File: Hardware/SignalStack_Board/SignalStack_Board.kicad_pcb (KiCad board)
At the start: 2 copper layers, 101.6 x 67.6 mm, 66 parts, among them J1 Molex_uF_SV_06, J2 RJ45_LED_Shielded, J3 Molex_uF_SV_06, Q1 SI4156DY, Q2 SI4156DY, Q3 SI4156DY, Q4 SI4156DY, Q5 SI4156DY, Q6 SI4156DY, Q7 SI4156DY, Q8 SI4156DY, U1 OKI, U2 SMAJ12CA, U3 Teensy4.1_DEV-16771, U4 TSR_1-2450, U5 IRS2005S, U6 IRS2005S, U8 IRS2005S, U9 IRS2005S

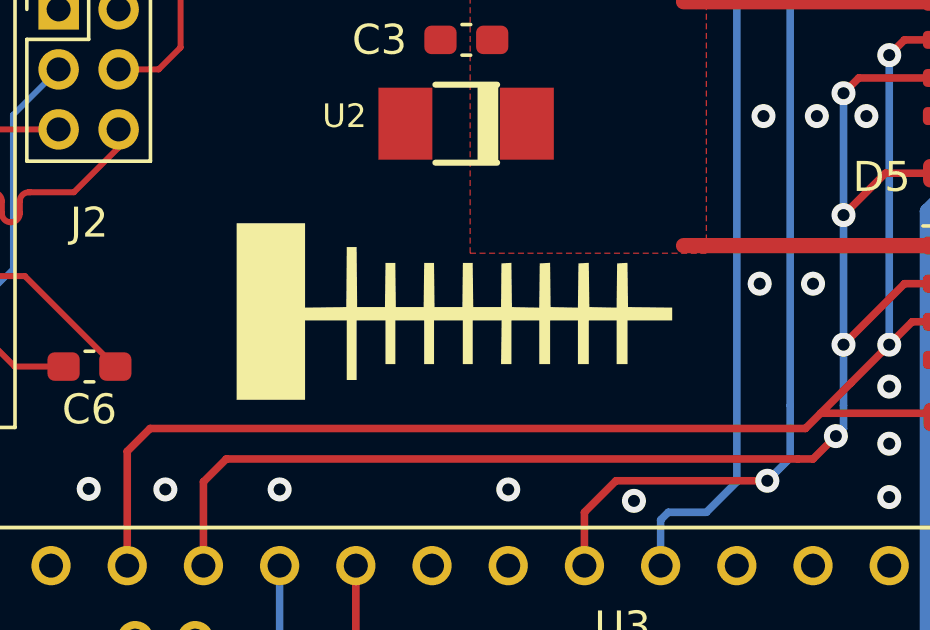
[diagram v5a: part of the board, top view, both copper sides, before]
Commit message: Changed yagi silkscreen
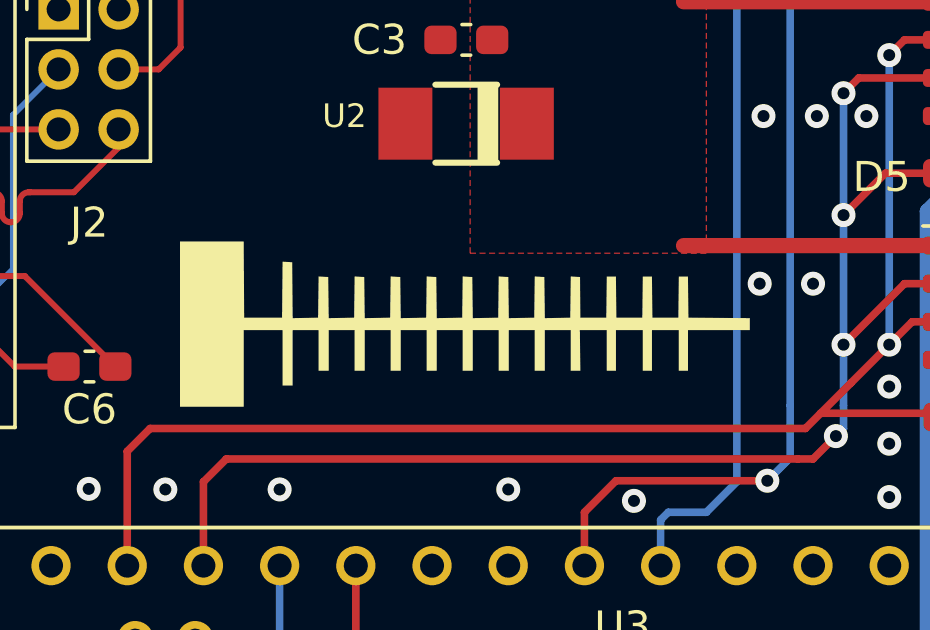
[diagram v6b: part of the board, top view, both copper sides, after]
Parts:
- moved G*** 0.63 mm to (188.3, 123.7)
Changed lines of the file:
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@@
     )
-  )
-  (footprint "MRDT_Silkscreens:yagi" (layer "F.Cu")
-    (at 187.96 123.19)
-    (attr board_only exclude_from_pos_files exclude_from_bom)
-    (fp_text reference "G***" (at 0 0) (layer "F.SilkS") hide
-      (effects (font (size 1.524 1.524) (thickness 0.3)))
-    )
-    (fp_text value "LOGO" (at 0.75 0) (layer "F.SilkS") hide
-      (effects (font (size 1.524 1.524) (thickness 0.3)))
-    )
-    (fp_poly (pts
-        (xy -4.994011 0.034415)
-        (xy -4.307748 0.025475)
-        (xy -3.621485 0.016536)
-        (xy -3.612732 -0.98392)
-        (xy -3.603978 -1.984375)
-        (xy -3.275189 -1.984375)
-        (xy -3.266436 -0.98392)
-        (xy -3.257683 0.016536)
-        (xy -2.331641 0.016536)
-        (xy -2.32274 -0.719336)
-        (xy -2.313839 -1.455209)
-        (xy -1.985641 -1.455209)
-        (xy -1.97674 -0.719336)
-        (xy -1.967839 0.016536)
-        (xy -1.041797 0.016536)
-        (xy -1.032896 -0.719336)
-        (xy -1.023995 -1.455209)
-        (xy -0.695797 -1.455209)
-        (xy -0.686896 -0.719336)
-        (xy -0.677995 0.016536)
-        (xy 0.248046 0.016536)
-        (xy 0.256947 -0.719336)
-        (xy 0.265848 -1.455209)
-        (xy 0.594047 -1.455209)
-        (xy 0.602948 -0.719336)
-        (xy 0.611849 0.016536)
-        (xy 1.53789 0.016536)
-        (xy 1.544146 -0.711068)
-        (xy 1.550401 -1.438672)
-        (xy 1.717141 -1.448647)
-        (xy 1.883881 -1.458621)
-        (xy 1.892787 -0.721042)
-        (xy 1.901692 0.016536)
-        (xy 2.35581 0.025734)
-        (xy 2.809927 0.034931)
-        (xy 2.818831 -0.701871)
-        (xy 2.827734 -1.438672)
-        (xy 3.000729 -1.448647)
-        (xy 3.173725 -1.458621)
-        (xy 3.182631 -0.721042)
-        (xy 3.191536 0.016536)
-        (xy 3.645653 0.025734)
-        (xy 4.099771 0.034931)
-        (xy 4.108674 -0.701871)
-        (xy 4.117578 -1.438672)
-        (xy 4.290573 -1.448647)
-        (xy 4.463569 -1.458621)
-        (xy 4.472474 -0.721042)
-        (xy 4.48138 0.016536)
-        (xy 4.935497 0.025734)
-        (xy 5.389615 0.034931)
-        (xy 5.398518 -0.701871)
-        (xy 5.407421 -1.438672)
-        (xy 5.580417 -1.448647)
-        (xy 5.753413 -1.458621)
-        (xy 5.762318 -0.721042)
-        (xy 5.771224 0.016536)
-        (xy 7.242968 0.034338)
-        (xy 7.242968 0.463021)
-        (xy 5.754687 0.463021)
-        (xy 5.754687 1.918229)
-        (xy 5.390885 1.918229)
-        (xy 5.390885 0.463021)
-        (xy 4.464843 0.463021)
-        (xy 4.464843 1.918229)
-        (xy 4.101041 1.918229)
-        (xy 4.101041 0.463021)
-        (xy 3.175 0.463021)
-        (xy 3.175 1.918229)
-        (xy 2.811198 1.918229)
-        (xy 2.811198 0.463021)
-        (xy 1.885156 0.463021)
-        (xy 1.885156 1.918229)
-        (xy 1.53789 1.918289)
-        (xy 1.556886 0.463021)
-        (xy 0.595312 0.463021)
-        (xy 0.595312 1.918229)
-        (xy 0.264583 1.918229)
-        (xy 0.264583 0.463021)
-        (xy -0.694532 0.463021)
-        (xy -0.694532 1.918229)
-        (xy -1.025261 1.918229)
-        (xy -1.025261 0.463021)
-        (xy -1.984375 0.463021)
-        (xy -1.984375 1.918229)
-        (xy -2.315105 1.918229)
-        (xy -2.315105 0.463021)
-        (xy -3.274219 0.463021)
-        (xy -3.274219 2.447396)
-        (xy -3.604948 2.447396)
-        (xy -3.604948 0.463021)
-        (xy -4.994011 0.463021)
-        (xy -4.994011 3.108854)
-        (xy -7.276042 3.108854)
-        (xy -7.276042 -2.778125)
-        (xy -4.994011 -2.778125)
-      ) (layer "F.SilkS") (width 0) (fill solid))
   )
   (footprint "MRDT_Shields:Teensy_4_1_Vertical" (layer "F.Cu")
@@
       (net 1 "+12V") (pintype "passive"))
   )
+  (footprint "MRDT_Silkscreens:yagi" (layer "F.Cu")
+    (at 188.341 123.698)
+    (attr board_only exclude_from_pos_files exclude_from_bom)
+    (fp_text reference "G***" (at 0 0) (layer "F.SilkS") hide
+      (effects (font (size 1.524 1.524) (thickness 0.3)))
+    )
+    (fp_text value "LOGO" (at 0.75 0) (layer "F.SilkS") hide
+      (effects (font (size 1.524 1.524) (thickness 0.3)))
+    )
+    (fp_poly (pts
+        (xy -7.412523 -1.408546)
+        (xy -7.404485 -0.138546)
+        (xy -6.142182 -0.138546)
+        (xy -6.134031 -1.071472)
+        (xy -6.12588 -2.004399)
+        (xy -5.964698 -1.995109)
+        (xy -5.803515 -1.985818)
+        (xy -5.795365 -1.053619)
+        (xy -5.787216 -0.12142)
+        (xy -4.941454 -0.138546)
+        (xy -4.933164 -0.825164)
+        (xy -4.924874 -1.511783)
+        (xy -4.763831 -1.502498)
+        (xy -4.602788 -1.493212)
+        (xy -4.5945 -0.807317)
+        (xy -4.586211 -0.121422)
+        (xy -3.740727 -0.138546)
+        (xy -3.732437 -0.825164)
+        (xy -3.724147 -1.511783)
+        (xy -3.563104 -1.502498)
+        (xy -3.402061 -1.493212)
+        (xy -3.393772 -0.807317)
+        (xy -3.385484 -0.121422)
+        (xy -2.54 -0.138546)
+        (xy -2.53171 -0.825164)
+        (xy -2.523419 -1.511783)
+        (xy -2.362376 -1.502498)
+        (xy -2.201333 -1.493212)
+        (xy -2.184757 -0.121422)
+        (xy -1.339273 -0.138546)
+        (xy -1.330982 -0.825164)
+        (xy -1.322692 -1.511783)
+        (xy -1.161649 -1.502498)
+        (xy -1.000606 -1.493212)
+        (xy -0.992318 -0.807317)
+        (xy -0.984029 -0.121422)
+        (xy -0.138545 -0.138546)
+        (xy -0.130255 -0.825164)
+        (xy -0.121965 -1.511783)
+        (xy 0.039078 -1.502498)
+        (xy 0.200121 -1.493212)
+        (xy 0.20841 -0.807317)
+        (xy 0.216698 -0.121422)
+        (xy 1.062182 -0.138546)
+        (xy 1.070472 -0.825164)
+        (xy 1.078762 -1.511783)
+        (xy 1.239805 -1.502498)
+        (xy 1.400849 -1.493212)
+        (xy 1.417425 -0.121422)
+        (xy 2.262909 -0.138546)
+        (xy 2.271199 -0.825164)
+        (xy 2.27949 -1.511783)
+        (xy 2.440533 -1.502498)
+        (xy 2.601576 -1.493212)
+        (xy 2.618152 -0.121422)
+        (xy 3.463636 -0.138546)
+        (xy 3.471927 -0.825164)
+        (xy 3.480217 -1.511783)
+        (xy 3.635437 -1.502498)
+        (xy 3.790656 -1.493212)
+        (xy 3.79648 -0.815879)
+        (xy 3.802303 -0.138546)
+        (xy 4.664364 -0.138546)
+        (xy 4.680936 -1.508606)
+        (xy 4.986458 -1.508606)
+        (xy 5.00303 -0.138546)
+        (xy 5.865091 -0.138546)
+        (xy 5.881663 -1.508606)
+        (xy 6.187186 -1.508606)
+        (xy 6.203758 -0.138546)
+        (xy 7.065818 -0.138546)
+        (xy 7.08239 -1.508606)
+        (xy 7.387913 -1.508606)
+        (xy 7.404485 -0.138546)
+        (xy 9.451879 -0.122322)
+        (xy 9.451879 0.277091)
+        (xy 7.389091 0.277091)
+        (xy 7.389091 1.631757)
+        (xy 7.081212 1.631757)
+        (xy 7.081212 0.277091)
+        (xy 6.188364 0.277091)
+        (xy 6.188364 1.631757)
+        (xy 5.880485 1.631757)
+        (xy 5.880485 0.277091)
+        (xy 4.987636 0.277091)
+        (xy 4.987636 1.631757)
+        (xy 4.679758 1.631757)
+        (xy 4.679758 0.277091)
+        (xy 3.784619 0.277091)
+        (xy 3.802303 1.631813)
+        (xy 3.640667 1.631785)
+        (xy 3.47903 1.631757)
+        (xy 3.47903 0.277091)
+        (xy 2.61697 0.277091)
+        (xy 2.61697 1.631757)
+        (xy 2.278303 1.631757)
+        (xy 2.278303 0.277091)
+        (xy 1.416243 0.277091)
+        (xy 1.416243 1.631757)
+        (xy 1.077576 1.631757)
+        (xy 1.077576 0.277091)
+        (xy 0.215515 0.277091)
+        (xy 0.215515 1.631757)
+        (xy -0.123151 1.631757)
+        (xy -0.123151 0.277091)
+        (xy -0.985212 0.277091)
+        (xy -0.985212 1.631757)
+        (xy -1.323879 1.631757)
+        (xy -1.323879 0.277091)
+        (xy -2.185939 0.277091)
+        (xy -2.185939 1.631757)
+        (xy -2.524606 1.631757)
+        (xy -2.524606 0.277091)
+        (xy -3.386667 0.277091)
+        (xy -3.386667 1.631757)
+        (xy -3.725333 1.631757)
+        (xy -3.725333 0.277091)
+        (xy -4.587394 0.277091)
+        (xy -4.587394 1.631757)
+        (xy -4.926061 1.631757)
+        (xy -4.926061 0.277091)
+        (xy -5.788121 0.277091)
+        (xy -5.788121 2.124363)
+        (xy -6.126788 2.124363)
+        (xy -6.126788 0.277091)
+        (xy -7.419879 0.277091)
+        (xy -7.419879 2.832485)
+        (xy -9.544242 2.832485)
+        (xy -9.544242 -2.678546)
+        (xy -7.420562 -2.678546)
+      ) (layer "F.SilkS") (width 0) (fill solid))
+  )
   (footprint "Resistor_SMD:R_0603_1608Metric_Pad0.98x0.95mm_HandSolder" (layer "F.Cu")

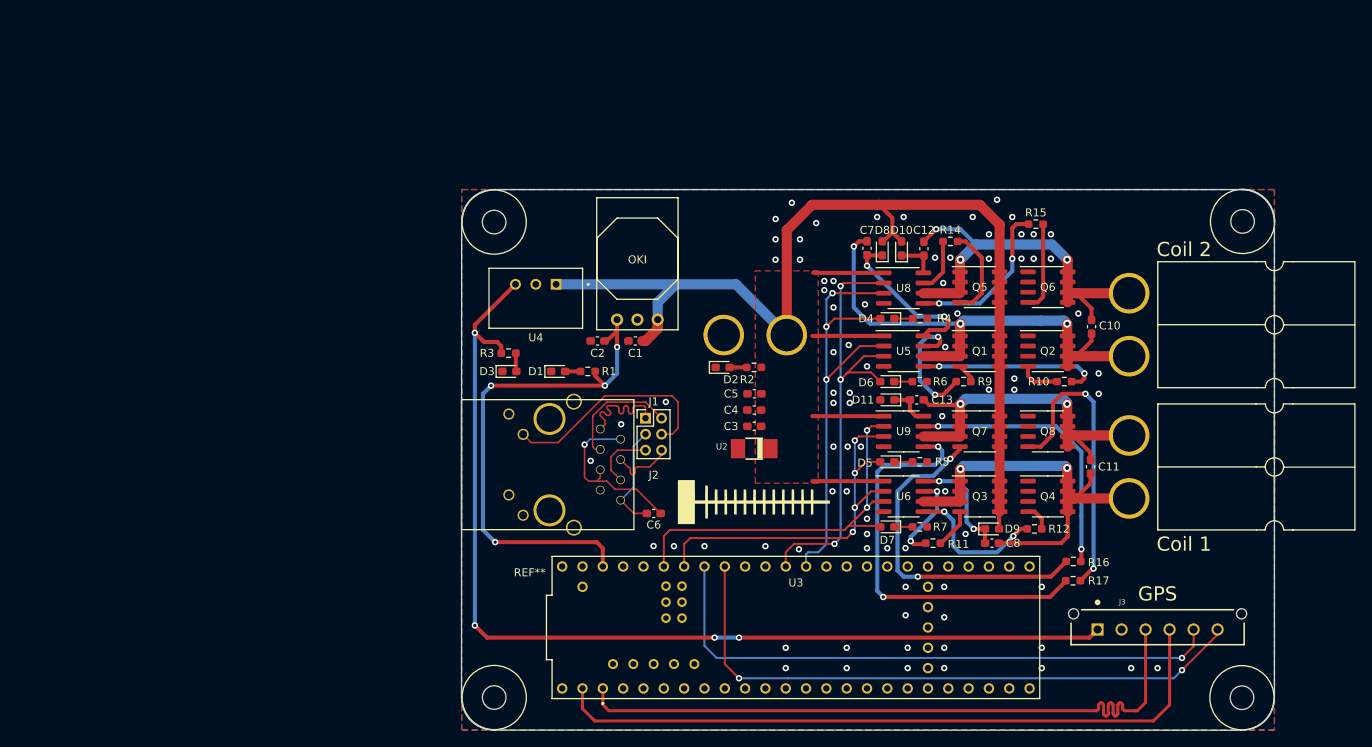
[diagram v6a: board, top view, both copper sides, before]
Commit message: Fixed dimensions
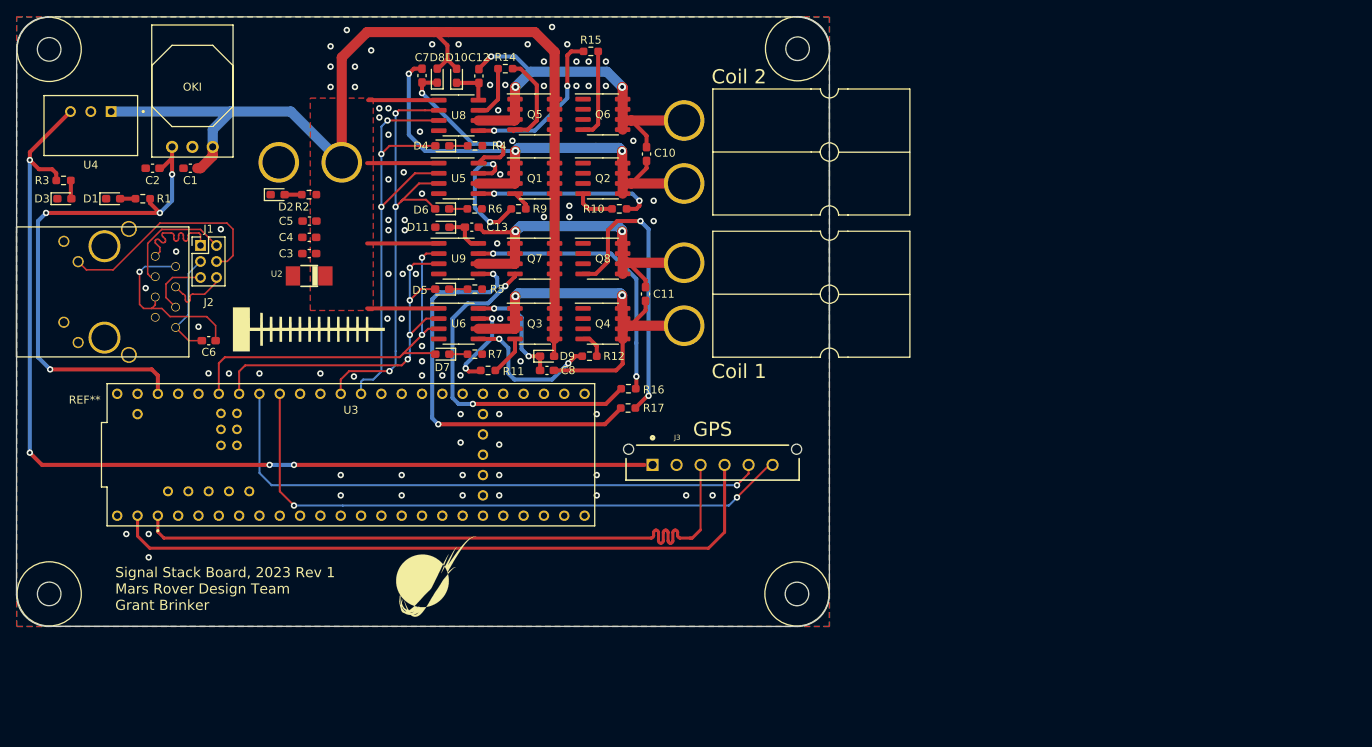
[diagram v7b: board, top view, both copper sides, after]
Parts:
- added G***: LOGO, MRDT_Silkscreens:0_MRDT_Logo_10mm, F.Cu at (148.6, 133.1)
- moved R3 59.7 mm to (102.0, 83.6)
- moved D1 59.7 mm to (108.2, 85.9)
- moved C1 59.7 mm to (117.9, 82.0)
- moved C10 59.7 mm to (174.9, 80.3)
- moved C12 59.7 mm to (153.9, 70.5)
- moved C13 59.7 mm to (153.0, 89.4)
- moved C3 59.7 mm to (132.7, 92.7)
- moved C4 59.7 mm to (132.7, 90.7)
- moved C5 59.7 mm to (132.7, 88.6)
- moved C6 59.7 mm to (120.2, 103.6)
- moved C8 59.7 mm to (162.4, 107.3)
- moved Conn1 59.7 mm to (128.9, 81.3)
- moved Conn2 59.7 mm to (179.6, 83.9)
- moved D10 59.7 mm to (151.1, 70.5)
- moved D11 59.7 mm to (149.4, 89.4)
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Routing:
- net +5V: track 128.5 -> 127.1 mm
- net Net-(C6-Pad1): track 21.8 -> 23.0 mm
- net I2C SCL: track 74.4 -> 73.4 mm
- net GPS RX: track 86.8 -> 85.8 mm
- net GPS TX: track 86.7 -> 85.6 mm
- net I2C SDA: track 77.4 -> 76.6 mm
- net GND: vias 81 -> 85
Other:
- board size 101.6 x 67.6 mm -> 101.6 x 76.2 mm

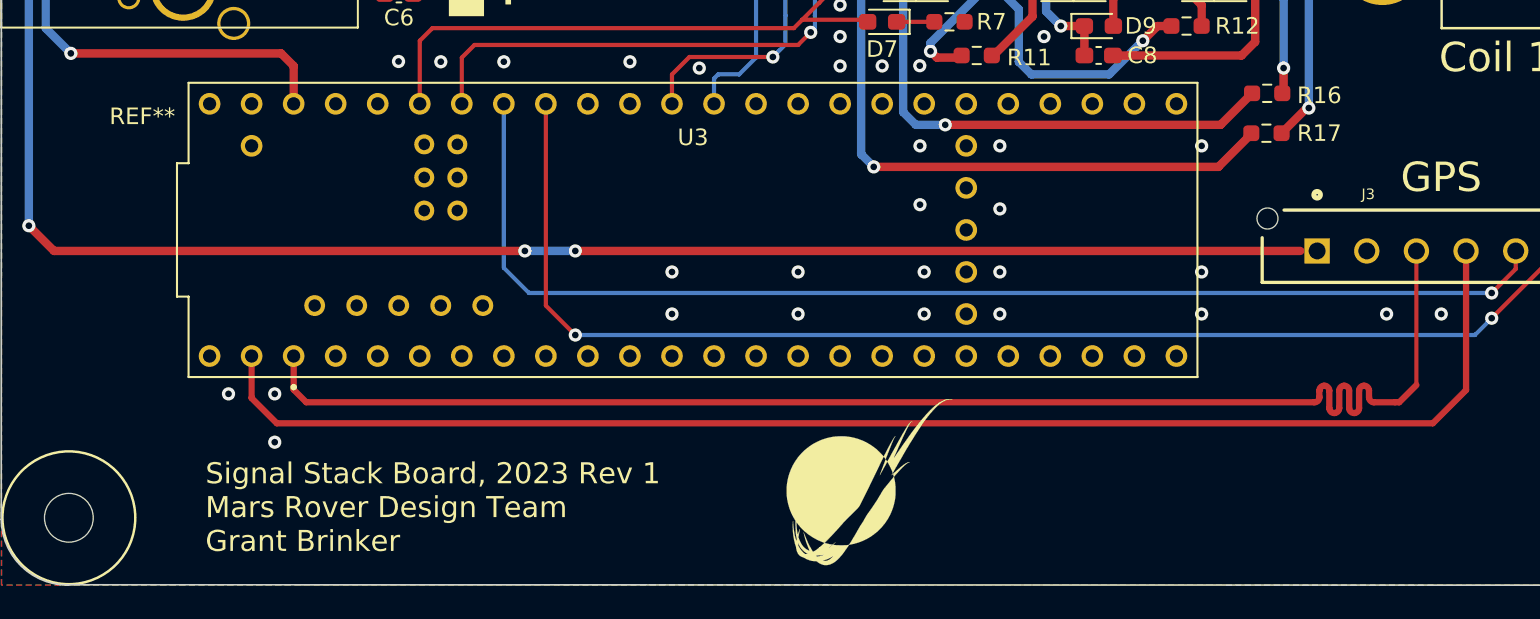
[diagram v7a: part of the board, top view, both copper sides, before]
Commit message: Added signature
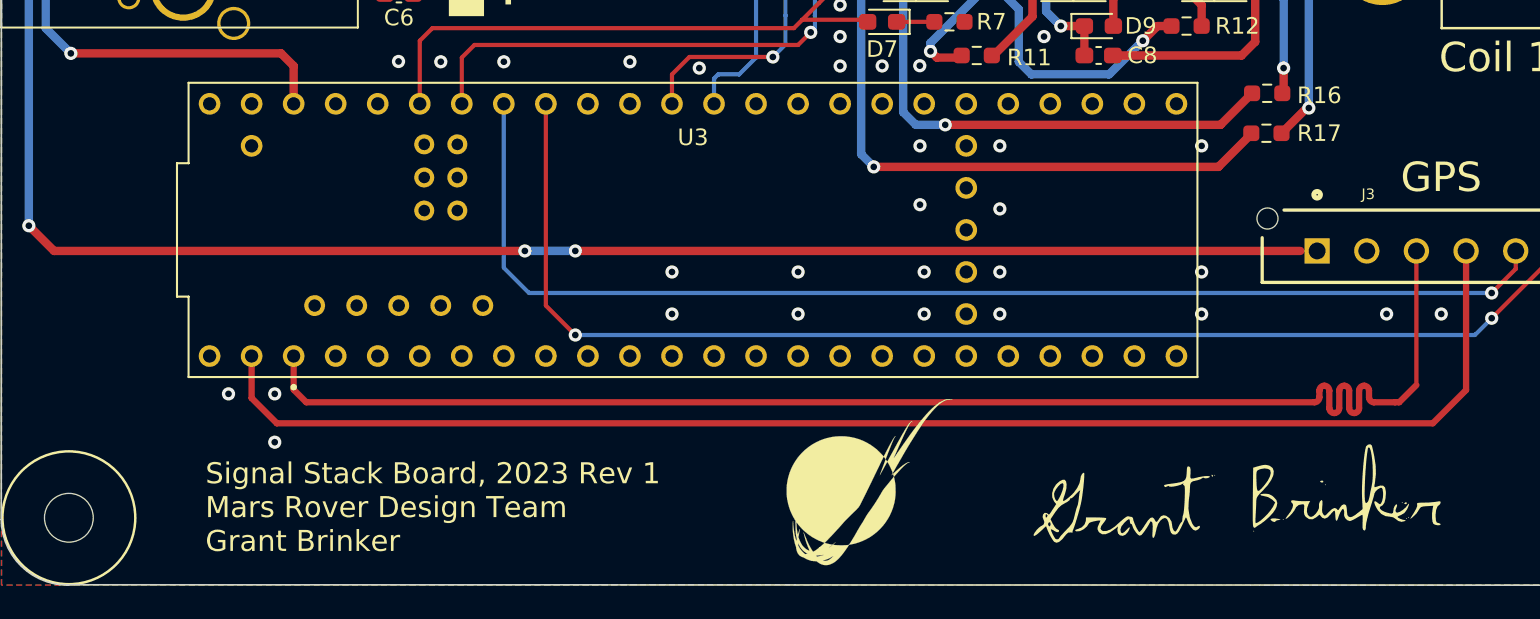
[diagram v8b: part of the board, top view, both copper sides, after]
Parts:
- added G***: LOGO, MRDT_Silkscreens:z_sig_Grant_Brinker_25mmx6, F.Cu at (170.9, 133.9)
